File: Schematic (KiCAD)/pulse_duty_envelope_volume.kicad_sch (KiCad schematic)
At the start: 75 parts, among them J65 Reg 4 D-Latch N, J68 Counter 4 Reset CL3

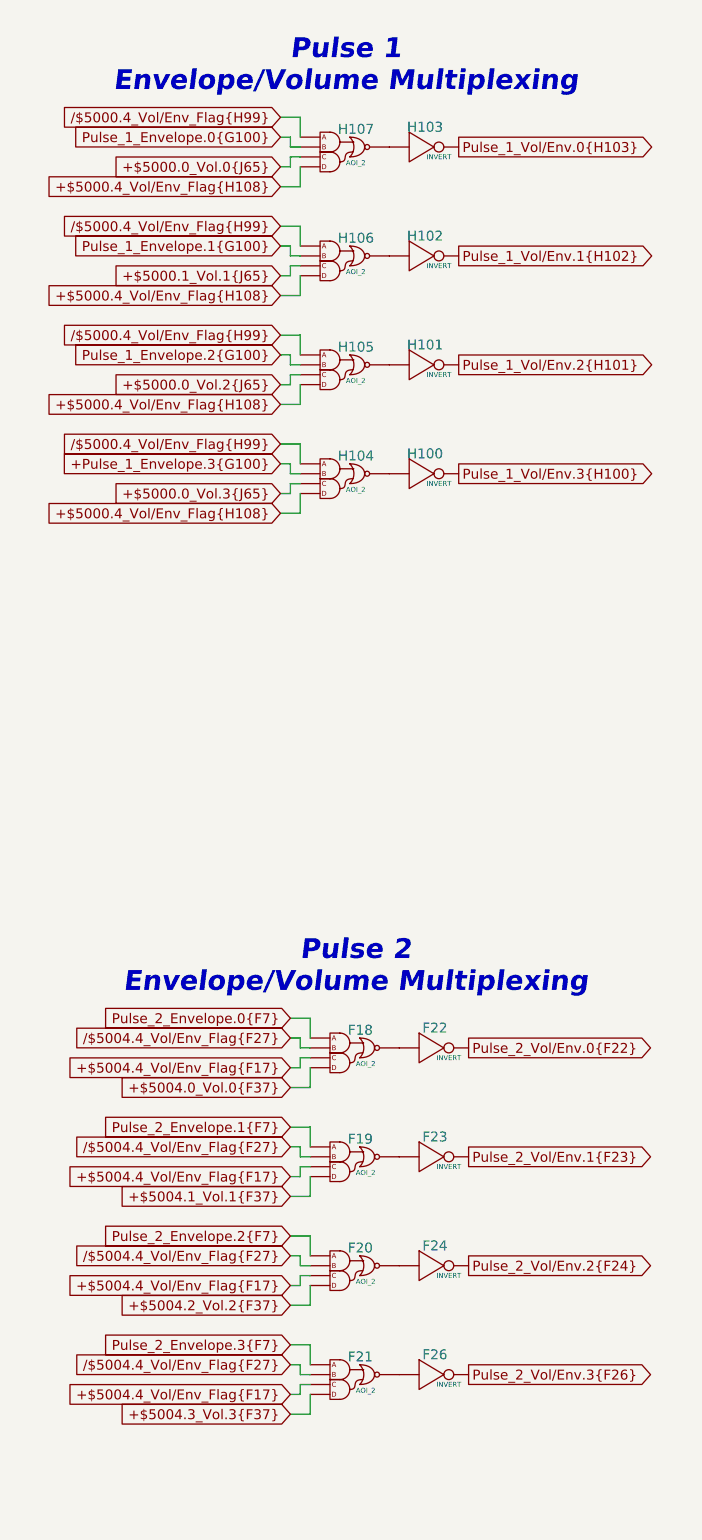
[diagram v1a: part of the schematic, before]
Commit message: - Updated all of the various And-OR-Invert gates to have consistent names.  - Added the schematic for CL3 / SL3 GPIO pins.  There are no surprises revealed by this.  - Finished up the CPU address decoding tracing.  - Added one of the 'artifact' counters from the pulse channels
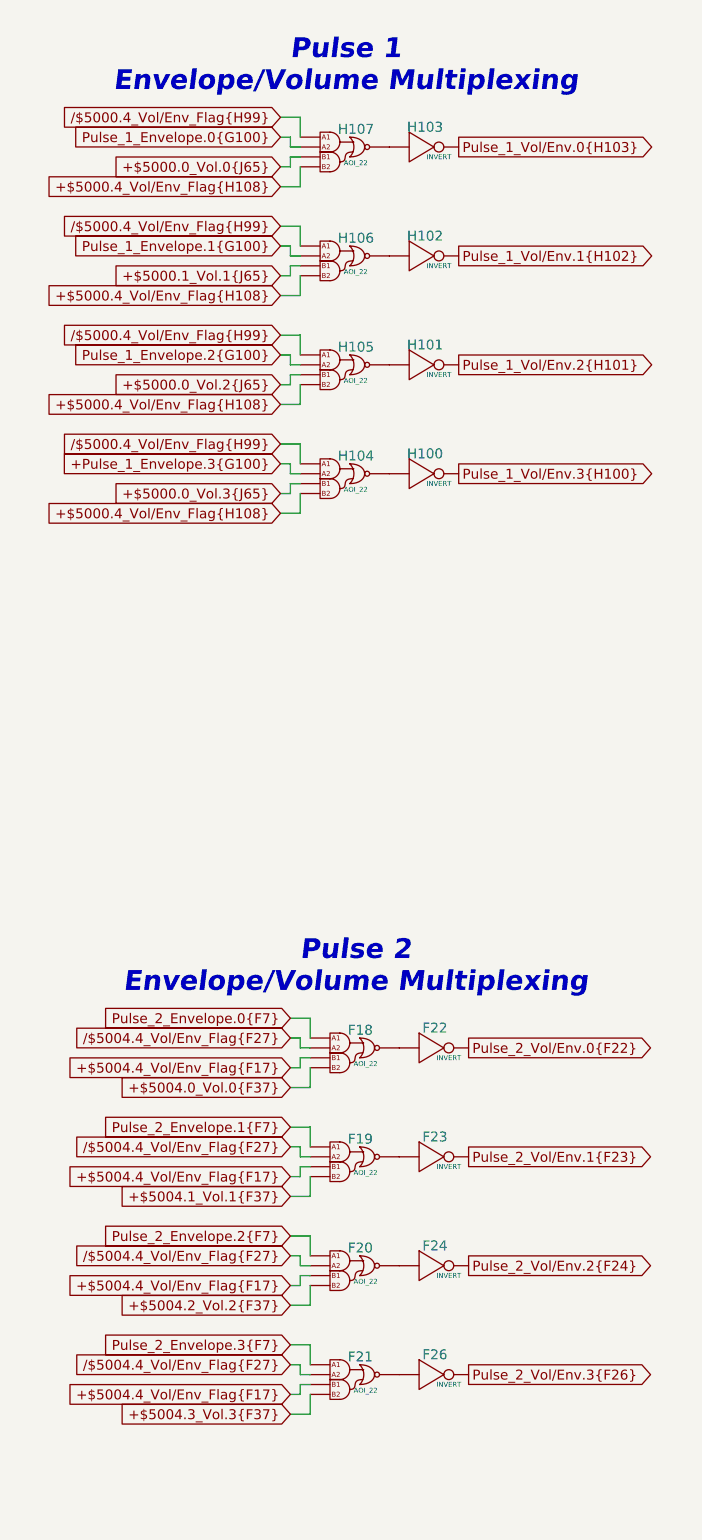
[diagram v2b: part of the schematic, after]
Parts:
- F18, F19, F20, F21, H104, H105, H106, H107: value AOI_2 -> AOI_22
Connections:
- net at H90. (X): now also G94. (X); no longer H89. (X)
- net at C36. (Y): now also B103. (X); no longer C34. (X)
- net at C35. (X): now also C33. (X); no longer C36. (Y)
- net at B103. (X): now also B104. (X), G20. (X); no longer C36. (Y)
- net at F36. (X): now also G97. (X); no longer F32. (X)
- net at C39. (X): now also C38. (X); no longer C41. (Y)
- net at E47. (X): now also F10. (X); no longer E48. (X)
- net at F15. (X): now also F16. (X); no longer G20. (X)
- net at G97. (X): now also G99. (X); no longer G98. (X)
- net at C41. (Y): now also C31(b). (/Q); no longer C40. (X)
- net at F16. (X): now also F13. (X); no longer F11. (X)
- new net: E45. (X), E46. (X), E47. (X), F12. (X)
- new net: F19. (X), F23. (X)
- new net: B99. (X), C38. (X)
- new net: H89. (X), H90. (X)
- new net: G99. (X), H90. (X), H91. (X), H92. (X)
- new net: C34. (X), C36. (Y)
- new net: C35. (X), C36. (Y)
- new net: C31(a). (/Q), C36. (Y)
- new net: H101. (X), H105. (X)
- new net: H100. (X), H104. (X)
- new net: F20. (X), F24. (X)
- new net: F32. (X), F36. (X)
- new net: B105. (X), B106. (X), F32. (X)
- new net: F35. (X), G85. (/Q3)
- new net: F34. (X), G85. (/Q3)
- new net: C39. (X), C41. (Y)
- new net: E47. (X), E48. (X)
- new net: F18. (X), F22. (X)
- new net: C37. (X), C38. (X)
- new net: F15. (X), G20. (X)
- new net: G97. (X), G98. (X)
- new net: C40. (X), C41. (Y)
- new net: H103. (X), H107. (X)
- new net: C32. (X), C33. (X)
- new net: H102. (X), H106. (X)
- new net: F11. (X), F16. (X)
- new net: G93. (X), G97. (X)
- new net: F21. (X), F26. (X)
- new net: E68. (/Q3), F7.1. (X)
- new net: E68. (/Q3), F8. (X)
- new net: G94. (X), G97. (X)
- new net: F10. (X), F16. (X)
- new net: F12. (X), F16. (X)
- new net: B100. (X), C33. (X)
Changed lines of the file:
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@@
 	)
 	(symbol
-		(lib_name "INVERT_17")
+		(lib_name "INVERT_8")
 		(lib_id "MMC5:INVERT")
 		(at 210.82 176.53 0)
@@
 	)
 	(symbol
-		(lib_name "INVERT_20")
+		(lib_name "INVERT_7")
 		(lib_id "MMC5:INVERT")
 		(at 379.73 161.29 0)
@@
 	)
 	(symbol
-		(lib_name "NOR_2_2")
 		(lib_id "MMC5:NOR_2")
 		(at 185.42 48.26 0)
@@
 	)
 	(symbol
-		(lib_name "UNKNOWN_2to2_1")
 		(lib_id "MMC5:UNKNOWN_2to2")
 		(at 232.41 214.63 0)
@@
 	)
 	(symbol
-		(lib_name "INVERT_36")
+		(lib_name "INVERT_6")
 		(lib_id "MMC5:INVERT")
 		(at 378.46 59.69 0)
@@
 	)
 	(symbol
-		(lib_name "INVERT_13")
+		(lib_name "INVERT_4")
 		(lib_id "MMC5:INVERT")
 		(at 78.74 64.77 0)
@@
 	)
 	(symbol
-		(lib_name "AOI_2_3")
 		(lib_id "MMC5:AOI_2")
 		(at 368.3 73.66 0)
@@
 			)
 		)
-		(property "Value" "AOI_2"
+		(property "Value" "AOI_22"
 			(at 369.062 75.692 0)
 			(do_not_autoplace yes)
@@
 	)
 	(symbol
-		(lib_name "INVERT_21")
+		(lib_name "INVERT_3")
 		(lib_id "MMC5:INVERT")
 		(at 379.73 175.26 0)
@@
 	)
 	(symbol
-		(lib_name "INVERT_32")
+		(lib_name "INVERT_9")
 		(lib_id "MMC5:INVERT")
 		(at 173.99 45.72 0)
@@
 	)
 	(symbol
-		(lib_name "INVERT_4")
 		(lib_id "MMC5:INVERT")
 		(at 69.85 59.69 0)
@@
 	)
 	(symbol
+		(lib_name "INVERT_10")
 		(lib_id "MMC5:INVERT")
 		(at 64.77 100.33 0)
@@
 	)
 	(symbol
-		(lib_name "INVERT_1")
+		(lib_name "INVERT_5")
 		(lib_id "MMC5:INVERT")
 		(at 64.77 85.09 0)
@@
 	)
 	(symbol
-		(lib_name "INVERT_31")
+		(lib_name "INVERT_11")
 		(lib_id "MMC5:INVERT")
 		(at 223.52 91.44 0)
@@
 	)
 	(symbol
-		(lib_name "NOR_2_6")
+		(lib_name "NOR_2_2")
 		(lib_id "MMC5:NOR_2")
 		(at 185.42 165.1 0)
@@
 	)
 	(symbol
-		(lib_name "Reg_4_D-Latch_N_1")
 		(lib_id "MMC5:Reg_4_D-Latch_N")
 		(at 49.53 52.07 0)
@@
 	)
 	(symbol
-		(lib_name "INVERT_6")
+		(lib_name "INVERT_12")
 		(lib_id "MMC5:INVERT")
 		(at 69.85 175.26 0)
@@
 	)
 	(symbol
-		(lib_name "INVERT_5")
+		(lib_name "INVERT_1")
 		(lib_id "MMC5:INVERT")
 		(at 78.74 180.34 0)
@@
 	)
 	(symbol
-		(lib_name "AOI_2_4")
+		(lib_name "AOI_2_1")
 		(lib_id "MMC5:AOI_2")
 		(at 369.57 147.32 0)
@@
 			)
 		)
-		(property "Value" "AOI_2"
+		(property "Value" "AOI_22"
 			(at 370.332 149.352 0)
 			(do_not_autoplace yes)
@@
 	)
 	(symbol
-		(lib_name "INVERT_33")
+		(lib_name "INVERT_2")
 		(lib_id "MMC5:INVERT")
 		(at 210.82 59.69 0)
@@
 	)
 	(symbol
-		(lib_name "INVERT_27")
+		(lib_name "INVERT_13")
 		(lib_id "MMC5:INVERT")
 		(at 203.2 91.44 0)
@@
 	)
 	(symbol
-		(lib_name "INVERT_15")
+		(lib_name "INVERT_14")
 		(lib_id "MMC5:INVERT")
 		(at 223.52 215.9 0)
@@
 	)
 	(symbol
-		(lib_name "NAND_3_8")
 		(lib_id "MMC5:NAND_3")
 		(at 219.71 54.61 0)
@@
 	)
 	(symbol
+		(lib_name "UNKNOWN_2to2_1")
 		(lib_id "MMC5:UNKNOWN_2to2")
 		(at 232.41 97.79 0)
@@
 	)
 	(symbol
-		(lib_name "INVERT_34")
+		(lib_name "INVERT_15")
 		(lib_id "MMC5:INVERT")
 		(at 378.46 31.75 0)
@@
 	)
 	(symbol
-		(lib_name "INVERT_3")
+		(lib_name "INVERT_16")
 		(lib_id "MMC5:INVERT")
 		(at 73.66 90.17 0)
@@
 	)
 	(symbol
-		(lib_name "INVERT_12")
+		(lib_name "INVERT_17")
 		(lib_id "MMC5:INVERT")
 		(at 203.2 208.28 0)
@@
 	)
 	(symbol
+		(lib_name "Reg_4_D-Latch_N_1")
 		(lib_id "MMC5:Reg_4_D-Latch_N")
 		(at 49.53 26.67 0)
@@
 	)
 	(symbol
-		(lib_name "AOI_2_1")
+		(lib_name "AOI_2_2")
 		(lib_id "MMC5:AOI_2")
 		(at 368.3 45.72 0)
@@
 			)
 		)
-		(property "Value" "AOI_2"
+		(property "Value" "AOI_22"
 			(at 369.062 47.752 0)
 			(do_not_autoplace yes)
@@
 	)
 	(symbol
-		(lib_name "NAND_2_2")
 		(lib_id "MMC5:NAND_2")
 		(at 173.99 168.91 0)
@@
 	)
 	(symbol
-		(lib_name "INVERT_19")
+		(lib_name "INVERT_25")
 		(lib_id "MMC5:INVERT")
 		(at 379.73 147.32 0)
@@
 	)
 	(symbol
-		(lib_name "NAND_3_4")
+		(lib_name "NAND_3_7")
 		(lib_id "MMC5:NAND_3")
 		(at 219.71 184.15 0)
@@
 	)
 	(symbol
+		(lib_name "NAND_3_6")
 		(lib_id "MMC5:NAND_3")
 		(at 219.71 67.31 0)
@@
 	)
 	(symbol
-		(lib_name "INVERT_28")
+		(lib_name "INVERT_19")
 		(lib_id "MMC5:INVERT")
 		(at 245.11 60.96 0)
@@
 	)
 	(symbol
-		(lib_name "INVERT_22")
+		(lib_name "INVERT_27")
 		(lib_id "MMC5:INVERT")
 		(at 379.73 189.23 0)
@@
 	)
 	(symbol
-		(lib_name "AOI_2_5")
+		(lib_name "AOI_2_4")
 		(lib_id "MMC5:AOI_2")
 		(at 369.57 175.26 0)
@@
 			)
 		)
-		(property "Value" "AOI_2"
+		(property "Value" "AOI_22"
 			(at 370.332 177.292 0)
 			(do_not_autoplace yes)
@@
 	)
 	(symbol
-		(lib_name "INVERT_18")
+		(lib_name "INVERT_29")
 		(lib_id "MMC5:INVERT")
 		(at 173.99 162.56 0)
@@
 	)
 	(symbol
-		(lib_name "INVERT_35")
+		(lib_name "INVERT_28")
 		(lib_id "MMC5:INVERT")
 		(at 378.46 45.72 0)
@@
 	)
 	(symbol
-		(lib_name "INVERT_11")
+		(lib_name "INVERT_30")
 		(lib_id "MMC5:INVERT")
 		(at 245.11 177.8 0)
@@
 	)
 	(symbol
-		(lib_name "INVERT_2")
+		(lib_name "INVERT_22")
 		(lib_id "MMC5:INVERT")
 		(at 73.66 105.41 0)
@@
 	)
 	(symbol
-		(lib_name "NAND_3_7")
+		(lib_name "NAND_3_2")
 		(lib_id "MMC5:NAND_3")
 		(at 219.71 45.72 0)
@@
 	)
 	(symbol
+		(lib_name "AOI_2_3")
 		(lib_id "MMC5:AOI_2")
 		(at 368.3 31.75 0)
@@
 			)
 		)
-		(property "Value" "AOI_2"
+		(property "Value" "AOI_22"
 			(at 369.062 33.782 0)
 			(do_not_autoplace yes)
@@
 	)
 	(symbol
-		(lib_name "INVERT_29")
+		(lib_name "INVERT_24")
 		(lib_id "MMC5:INVERT")
 		(at 245.11 96.52 0)
@@
 	)
 	(symbol
-		(lib_name "INVERT_9")
+		(lib_name "INVERT_18")
 		(lib_id "MMC5:INVERT")
 		(at 64.77 215.9 0)
@@
 	)
 	(symbol
-		(lib_name "NAND_3_2")
+		(lib_name "NAND_3_4")
 		(lib_id "MMC5:NAND_3")
 		(at 219.71 162.56 0)
@@
 	)
 	(symbol
-		(lib_name "NOR_3_3")
 		(lib_id "MMC5:NOR_3")
 		(at 212.09 91.44 0)
@@
 	)
 	(symbol
-		(lib_name "INVERT_23")
+		(lib_name "INVERT_35")
 		(lib_id "MMC5:INVERT")
 		(at 254 213.36 0)
@@
 	)
 	(symbol
-		(lib_name "INVERT_7")
+		(lib_name "INVERT_20")
 		(lib_id "MMC5:INVERT")
 		(at 73.66 205.74 0)
@@
 	)
 	(symbol
-		(lib_name "INVERT_30")
+		(lib_name "INVERT_23")
 		(lib_id "MMC5:INVERT")
 		(at 223.52 99.06 0)
@@
 	)
 	(symbol
-		(lib_name "INVERT_24")
+		(lib_name "INVERT_34")
 		(lib_id "MMC5:INVERT")
 		(at 254 96.52 0)
@@
 	)
 	(symbol
-		(lib_name "NAND_3_5")
+		(lib_name "NAND_3_1")
 		(lib_id "MMC5:NAND_3")
 		(at 219.71 193.04 0)
@@
 	)
 	(symbol
-		(lib_name "INVERT_10")
+		(lib_name "INVERT_26")
 		(lib_id "MMC5:INVERT")
 		(at 64.77 200.66 0)
@@
 	)
 	(symbol
-		(lib_name "INVERT_16")
+		(lib_name "INVERT_31")
 		(lib_id "MMC5:INVERT")
 		(at 223.52 208.28 0)
@@
 	)
 	(symbol
-		(lib_name "AOI_2_7")
+		(lib_name "AOI_2_5")
 		(lib_id "MMC5:AOI_2")
 		(at 369.57 189.23 0)
@@
 			)
 		)
-		(property "Value" "AOI_2"
+		(property "Value" "AOI_22"
 			(at 370.332 191.262 0)
 			(do_not_autoplace yes)
@@
 	)
 	(symbol
-		(lib_name "INVERT_8")
+		(lib_name "INVERT_32")
 		(lib_id "MMC5:INVERT")
 		(at 73.66 220.98 0)
@@
 	)
 	(symbol
-		(lib_name "INVERT_14")
+		(lib_name "INVERT_21")
 		(lib_id "MMC5:INVERT")
 		(at 245.11 213.36 0)
@@
 	)
 	(symbol
-		(lib_name "NAND_3_1")
+		(lib_name "NAND_3_5")
 		(lib_id "MMC5:NAND_3")
 		(at 219.71 76.2 0)
@@
 	)
 	(symbol
-		(lib_name "AOI_2_6")
+		(lib_name "AOI_2_7")
 		(lib_id "MMC5:AOI_2")
 		(at 369.57 161.29 0)
@@
 			)
 		)
-		(property "Value" "AOI_2"
+		(property "Value" "AOI_22"
 			(at 370.332 163.322 0)
 			(do_not_autoplace yes)
@@
 	)
 	(symbol
-		(lib_name "AOI_2_2")
+		(lib_name "AOI_2_6")
 		(lib_id "MMC5:AOI_2")
 		(at 368.3 59.69 0)
@@
 			)
 		)
-		(property "Value" "AOI_2"
+		(property "Value" "AOI_22"
 			(at 369.062 61.722 0)
 			(do_not_autoplace yes)
@@
 	)
 	(symbol
-		(lib_name "INVERT_37")
+		(lib_name "INVERT_33")
 		(lib_id "MMC5:INVERT")
 		(at 378.46 73.66 0)
